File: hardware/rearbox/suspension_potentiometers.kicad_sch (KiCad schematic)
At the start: 0 parts

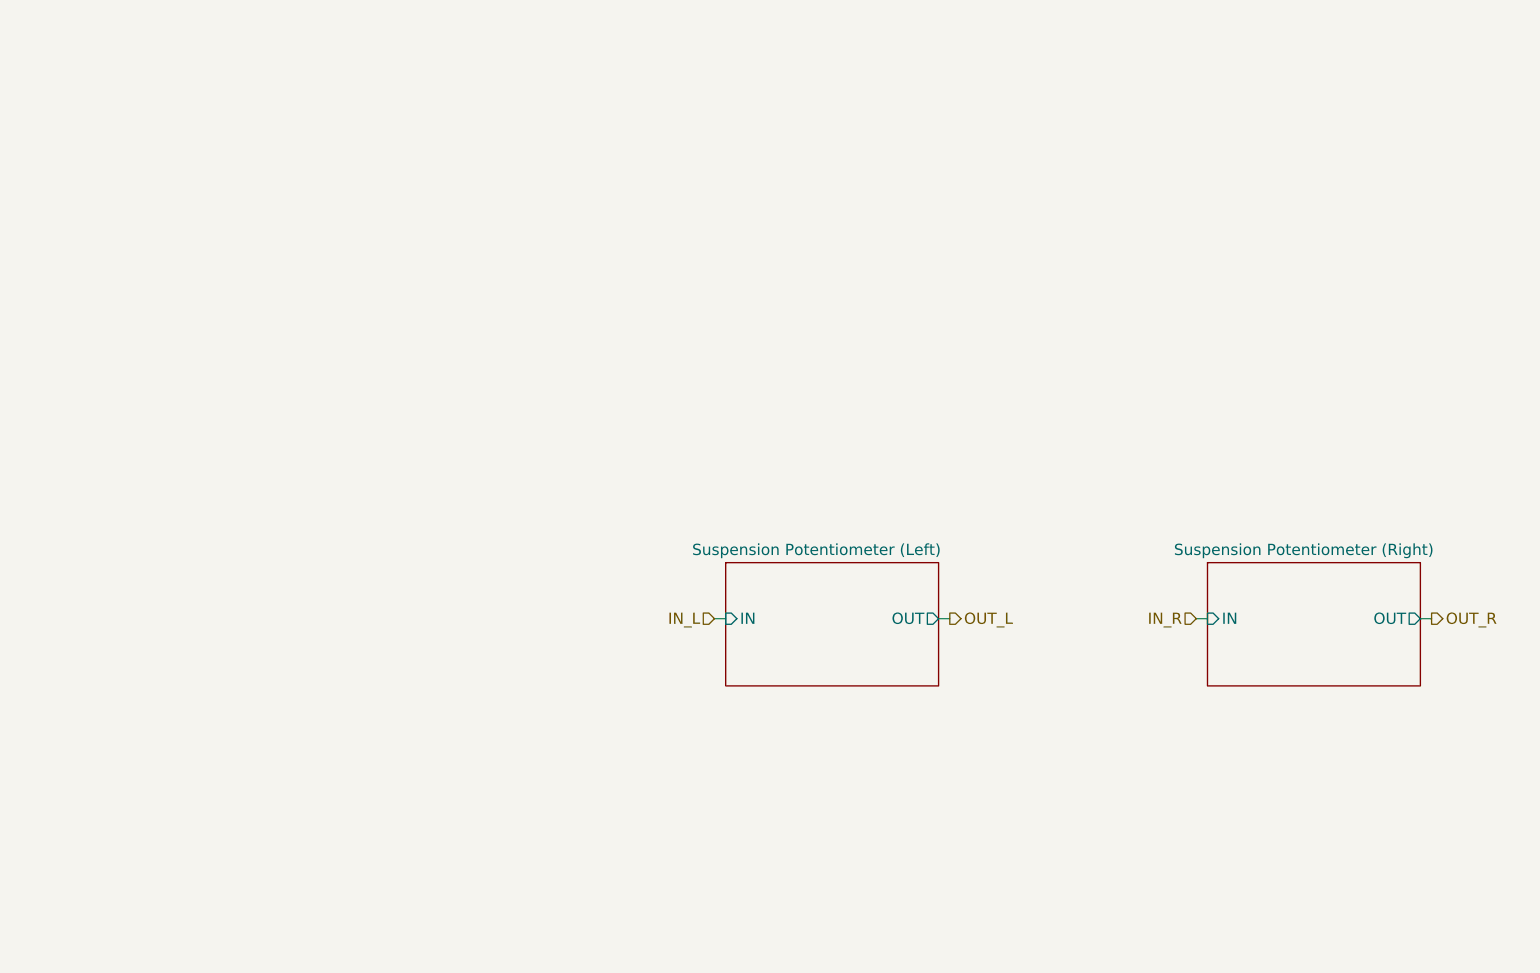
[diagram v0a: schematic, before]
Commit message: Place components on the PCB
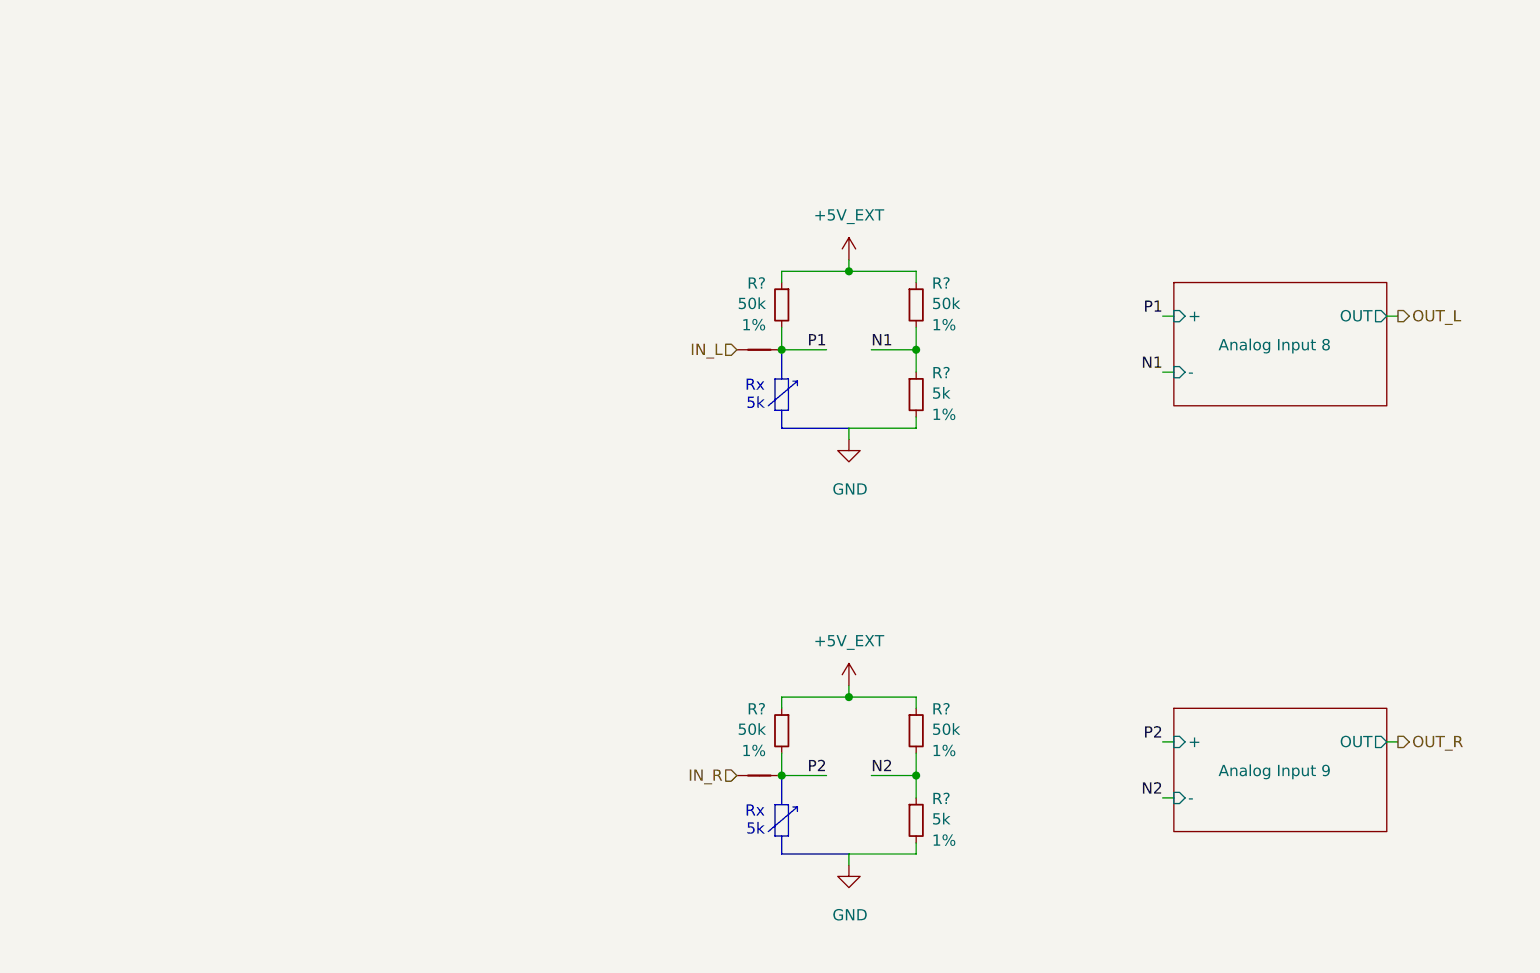
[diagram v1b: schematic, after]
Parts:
- added NT8, NT9: NetTie_2, NetTie:NetTie-2_SMD_Pad0.5mm, symbol Device:NetTie_2
- added R? (x4): 50k, Resistor_SMD:R_0603_1608Metric, symbol Device:R_Small
- added R? (x2): 5k, Resistor_SMD:R_0603_1608Metric, symbol Device:R_Small
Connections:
- net IN_L: now also NT8.1
- net IN_R: now also NT9.1
- new net +5V_EXT: R?.1, R?.1, R?.1, R?.1
- new net GND: R?.2, R?.2
- new net N1: R?.1, R?.2
- new net N2: R?.1, R?.2
- new net P1: NT8.2, R?.2
- new net P2: NT9.2, R?.2
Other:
- removed sheet Suspension Potentiometer (Left)
- removed sheet Suspension Potentiometer (Right)
- added sheet Analog Input 8 (analog_input.kicad_sch)
- added sheet Analog Input 9 (analog_input.kicad_sch)
- note added: "Rx 5k"

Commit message: Fix DRCs
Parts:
- NT8, NT9: footprint NetTie:NetTie-2_SMD_Pad0.5mm -> Local_Library:NetTie-2_SMD_Pad0.2mm
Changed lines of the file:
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@@
   (title_block
     (title "Suspension Potentiometers")
-    (date "2023-11-02")
+    (date "2023-11-17")
     (rev "${REVISION}")
     (company "Author: I. Kajdan")
@@
       (effects (font (size 1.27 1.27)) hide)
     )
-    (property "Footprint" "NetTie:NetTie-2_SMD_Pad0.5mm" (at 111.76 121.92 0)
+    (property "Footprint" "Local_Library:NetTie-2_SMD_Pad0.2mm" (at 111.76 121.92 0)
       (effects (font (size 1.27 1.27)) hide)
     )
@@
       (effects (font (size 1.27 1.27)) hide)
     )
-    (property "Footprint" "NetTie:NetTie-2_SMD_Pad0.5mm" (at 111.76 73.66 0)
-      (effects (font (size 1.27 1.27)) hide)
-    )
+    (property "Footprint" "Local_Library:NetTie-2_SMD_Pad0.2mm" (at 111.76 73.66 0)
+      (effects (font (size 1.27 1.27)) hide)
+    )

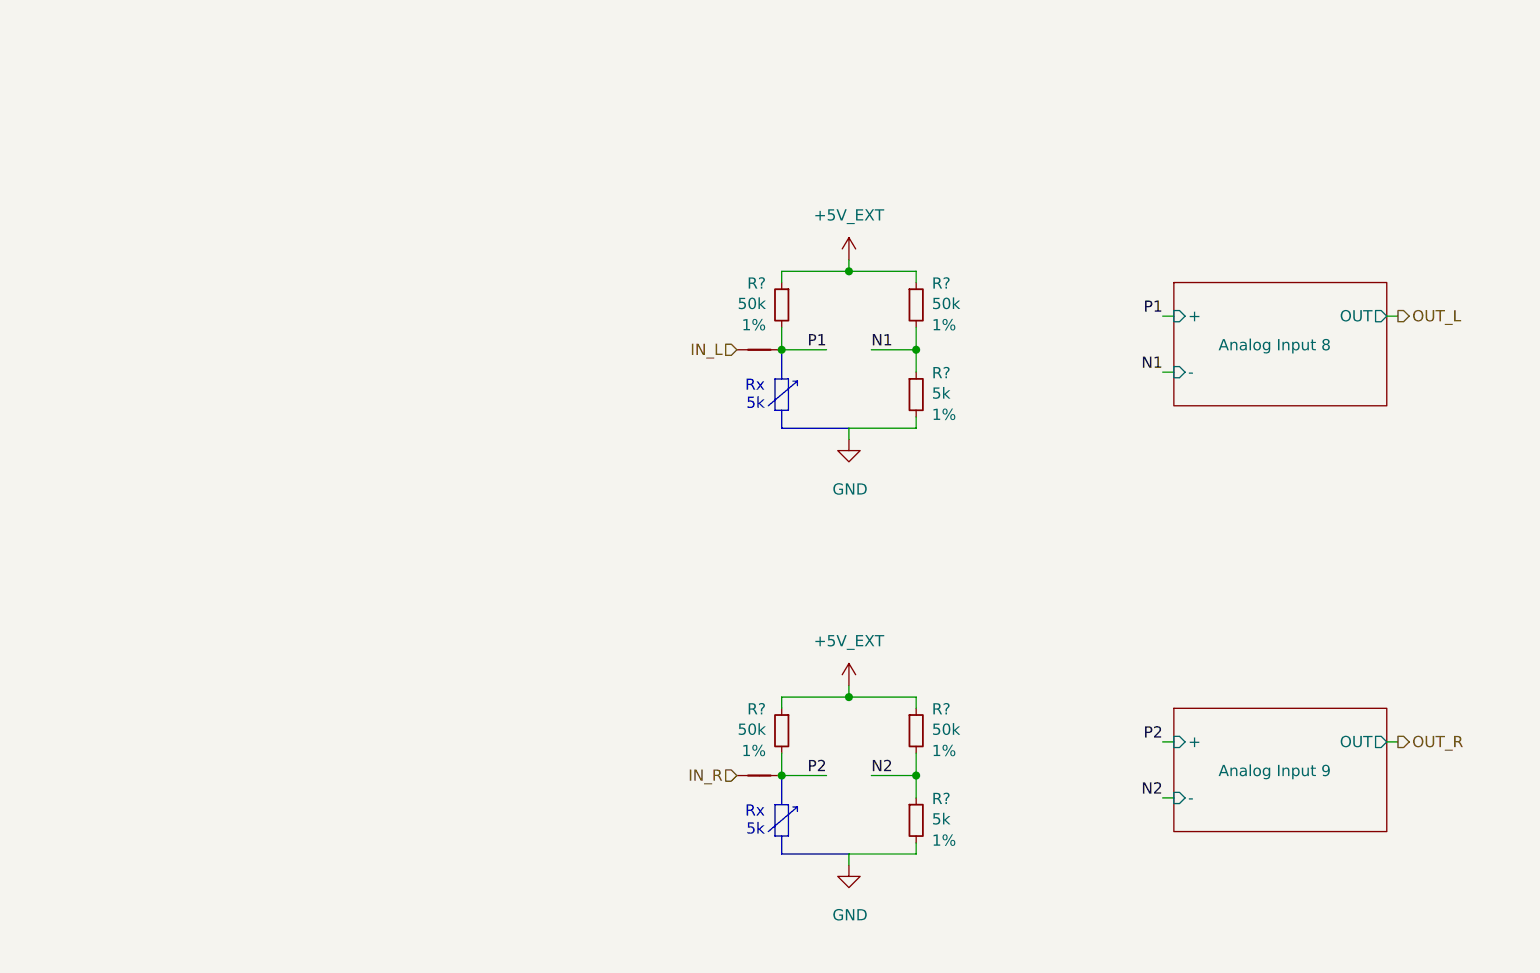
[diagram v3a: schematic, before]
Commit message: Route the tracks on the connector PCB
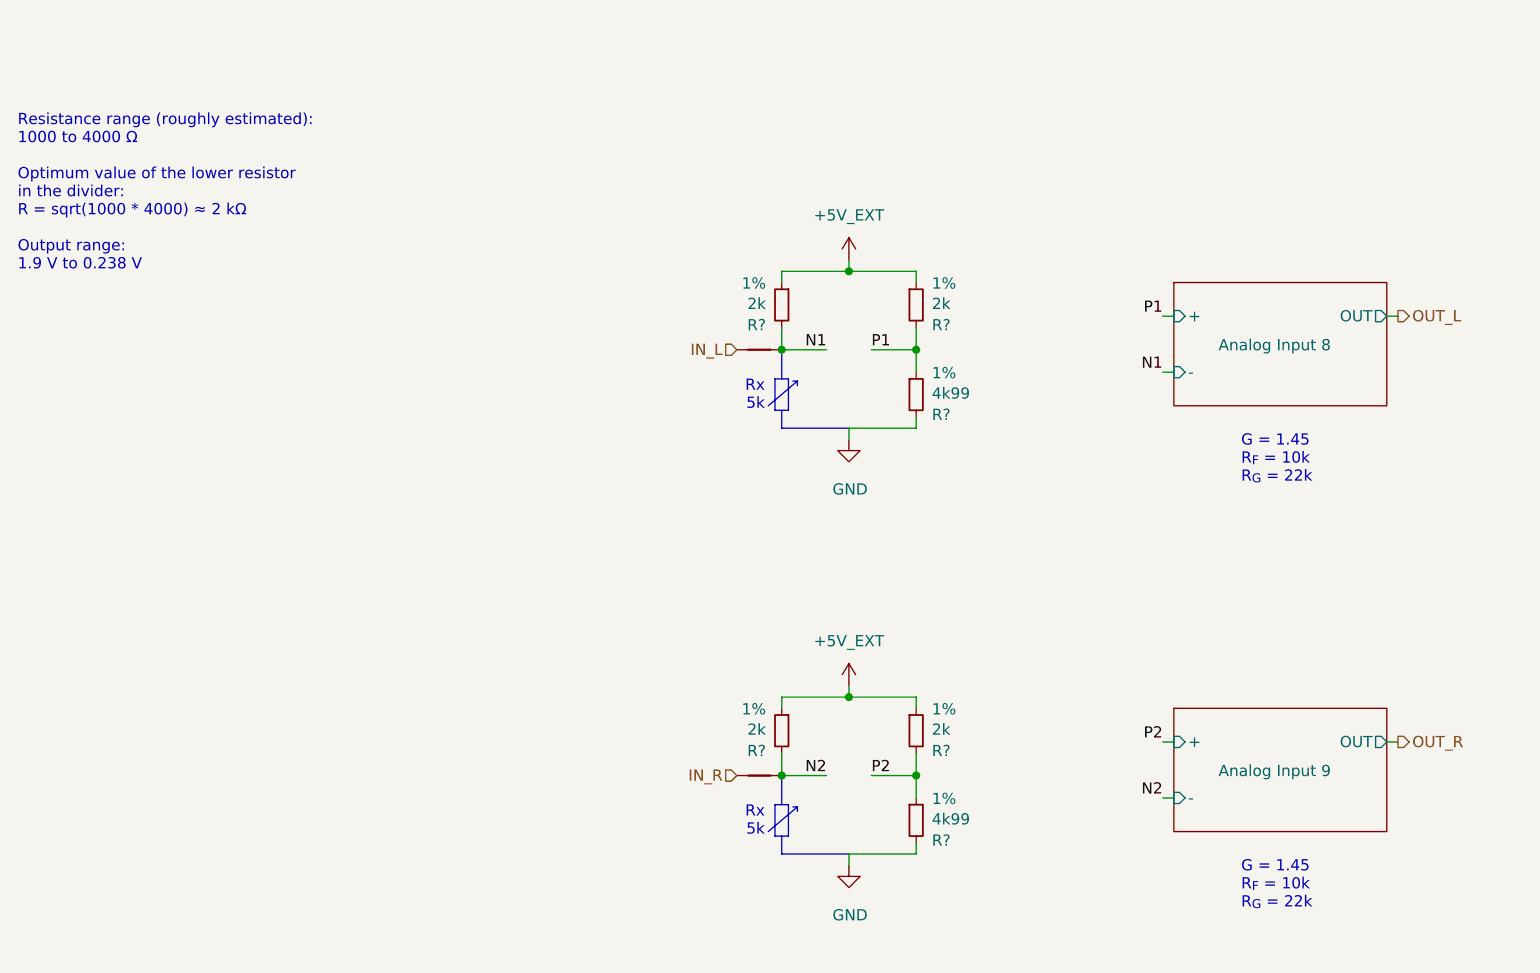
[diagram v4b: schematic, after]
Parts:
- R? (x4): value 50k -> 2k
- R? (x2): value 5k -> 4k99
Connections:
- net N1: now also NT8.2, R?.2; no longer R?.1, R?.2
- net N2: now also NT9.2, R?.2; no longer R?.1, R?.2
- net P1: now also R?.1, R?.2; no longer NT8.2, R?.2
- net P2: now also R?.1, R?.2; no longer NT9.2, R?.2
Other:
- note added: "G = 1.45 R_{F} = 10k R_{G} = 22k"

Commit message: Fix measurement bridges polarity
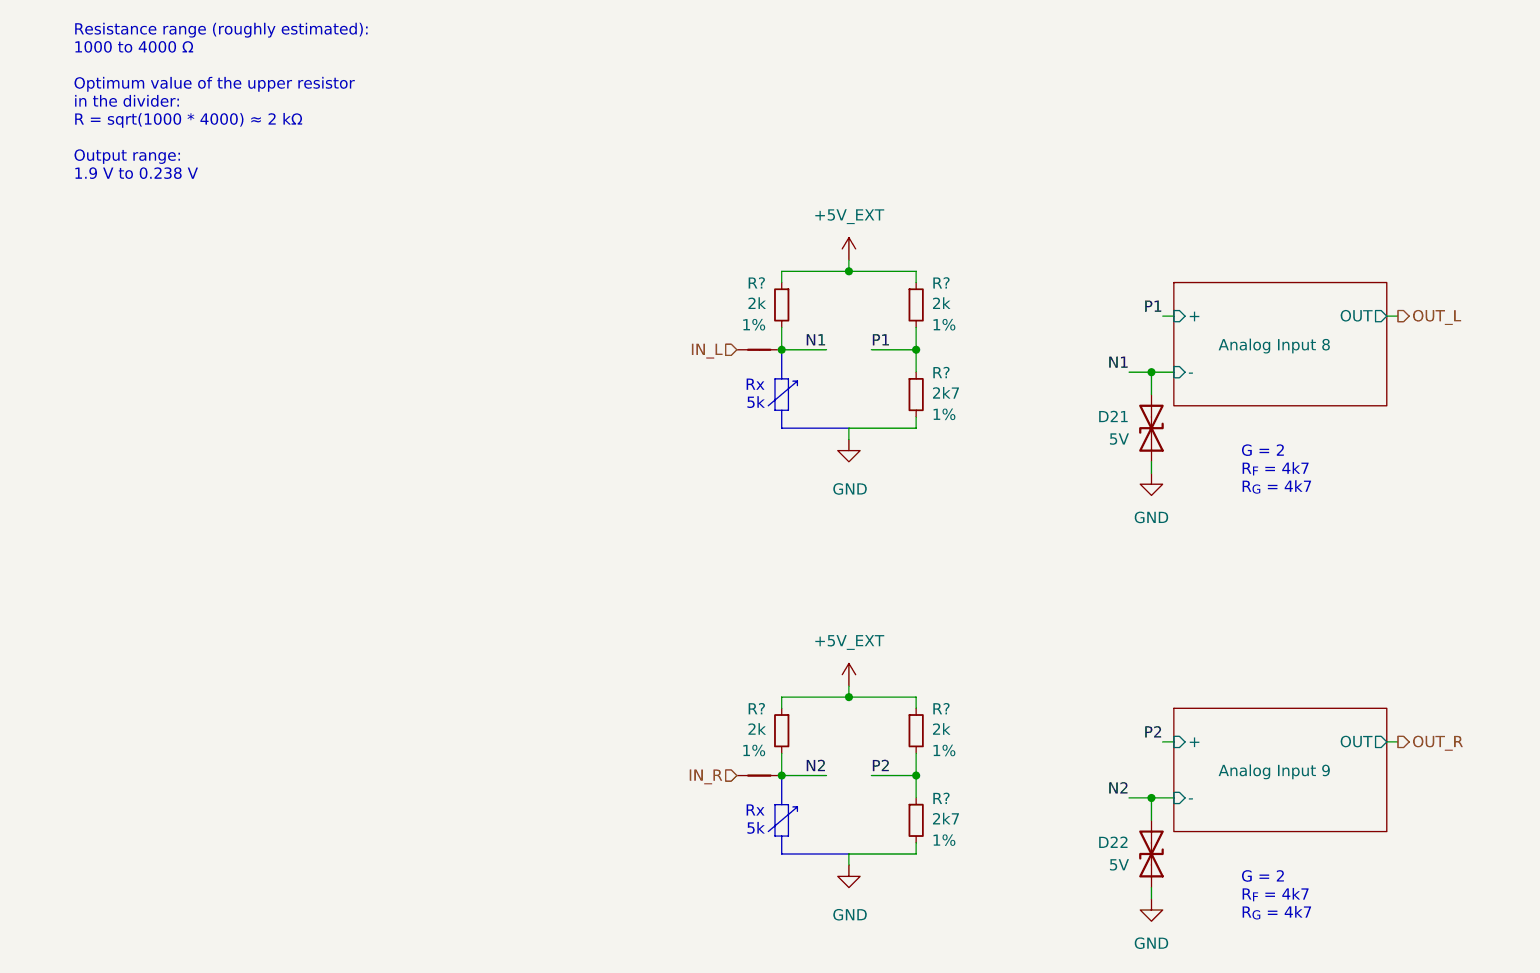
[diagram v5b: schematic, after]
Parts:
- added D21, D22: 5V, Diode_SMD:D_SOD-523, symbol Device:D_TVS
- R? (x2): value 4k99 -> 2k7
- renumbered NT8 to NT4, NT9 to NT5
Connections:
- net GND: now also D21.1 (A1), D22.1 (A1)
- net N1: now also D21.2 (A2)
- net N2: now also D22.2 (A2)
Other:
- note added: "G = 2 R_{F} = 4k7 R_{G} = 4k7"
- note removed: "G = 1.45 R_{F} = 10k R_{G} = 22k"
